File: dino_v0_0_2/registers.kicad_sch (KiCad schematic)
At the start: 5 parts, among them U31 74LS373, U32 74LS373, U33 74LS373, U34 74LS373, U35 74LS373

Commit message: Schematics WIP
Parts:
- removed U34: 74LS373, symbol 74xx:74LS373
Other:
- moved on the sheet: U35
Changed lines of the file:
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@@
-	(symbol
-		(lib_id "74xx:74LS373")
-		(at 181.61 102.87 0)
-		(mirror y)
-		(unit 1)
-		(exclude_from_sim no)
-		(in_bom yes)
-		(on_board yes)
-		(dnp no)
-		(property "Reference" "U34"
-			(at 179.4667 82.55 0)
-			(effects
-				(font
-					(size 1.27 1.27)
-				)
-				(justify left)
-			)
-		)
-		(property "Value" "74LS373"
-			(at 179.4667 85.09 0)
-			(effects
-				(font
-					(size 1.27 1.27)
-				)
-				(justify left)
-			)
-		)
-		(property "Footprint" ""
-			(at 181.61 102.87 0)
-			(effects
-				(font
-					(size 1.27 1.27)
-				)
-				(hide yes)
-			)
-		)
-		(property "Datasheet" "http://www.ti.com/lit/gpn/sn74LS373"
-			(at 181.61 102.87 0)
-			(effects
-				(font
-					(size 1.27 1.27)
-				)
-				(hide yes)
-			)
-		)
-		(property "Description" "8-bit Latch, 3-state outputs"
-			(at 181.61 102.87 0)
-			(effects
-				(font
-					(size 1.27 1.27)
-				)
-				(hide yes)
-			)
-		)
-		(pin "13"
-		)
-		(pin "14"
-		)
-		(pin "17"
-		)
-		(pin "18"
-		)
-		(pin "9"
-		)
-		(pin "12"
-		)
-		(pin "15"
-		)
-		(pin "16"
-		)
-		(pin "19"
-		)
-		(pin "11"
-		)
-		(pin "1"
-		)
-		(pin "20"
-		)
-		(pin "10"
-		)
-		(pin "2"
-		)
-		(pin "5"
-		)
-		(pin "6"
-		)
-		(pin "7"
-		)
-		(pin "8"
-		)
-		(pin "3"
-		)
-		(pin "4"
-		)
-		(instances
-			(project "dino_v0_0_2"
-				(path "/e43166a5-d972-471d-b3cf-9f4f12c7f541/de772b95-eca4-4f61-9f12-d1e28130490b"
-					(reference "U34")
-					(unit 1)
-				)
-			)
-		)
-	)
 	(symbol
 		(lib_id "74xx:74LS373")
@@
 	(symbol
 		(lib_id "74xx:74LS373")
-		(at 113.03 151.13 0)
+		(at 181.61 102.87 0)
+		(mirror y)
 		(unit 1)
 		(exclude_from_sim no)
@@
 		(on_board yes)
 		(dnp no)
-		(fields_autoplaced yes)
 		(property "Reference" "U35"
-			(at 115.1733 130.81 0)
+			(at 179.4667 82.55 0)
 			(effects
 				(font
@@
 		)
 		(property "Value" "74LS373"
-			(at 115.1733 133.35 0)
+			(at 179.4667 85.09 0)
 			(effects
 				(font
@@
 		)
 		(property "Footprint" ""
-			(at 113.03 151.13 0)
+			(at 181.61 102.87 0)
 			(effects
 				(font
@@
 		)
 		(property "Datasheet" "http://www.ti.com/lit/gpn/sn74LS373"
-			(at 113.03 151.13 0)
+			(at 181.61 102.87 0)
 			(effects
 				(font
@@
 		)
 		(property "Description" "8-bit Latch, 3-state outputs"
-			(at 113.03 151.13 0)
-			(effects
-				(font
+			(at 181.61 102.87 0)
+			(effects
+				(font

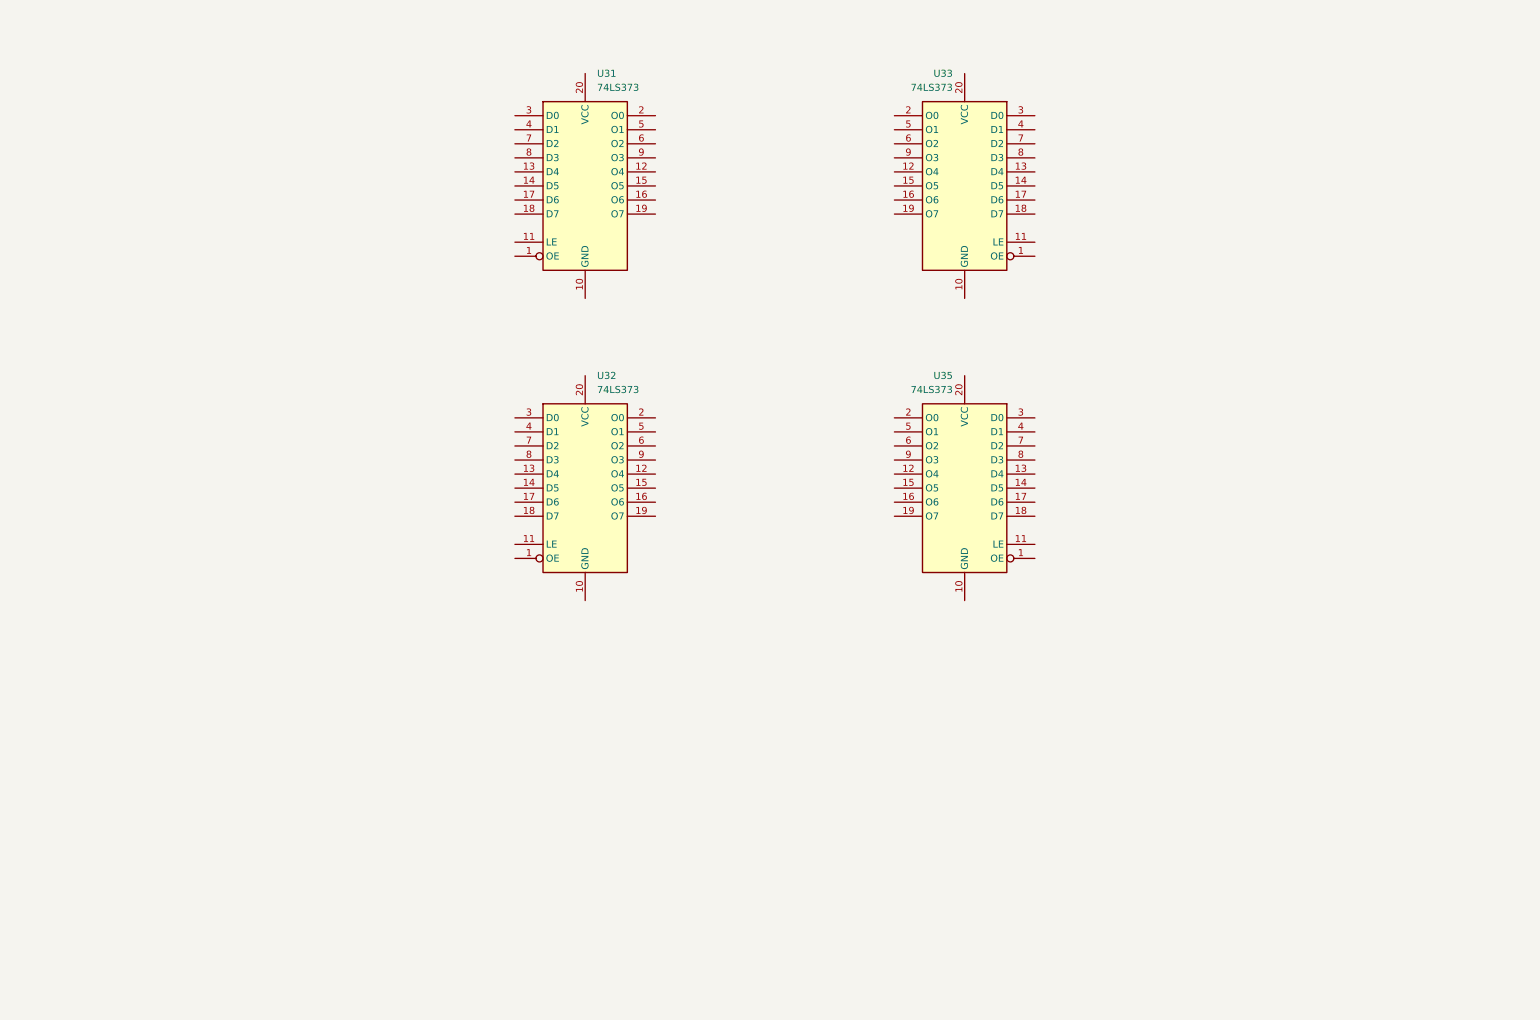
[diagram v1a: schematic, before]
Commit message: Update on Schematics
- Added the 74LS121 to the latches and RAM for intra phase pulses to allow for Latch/Write Enables
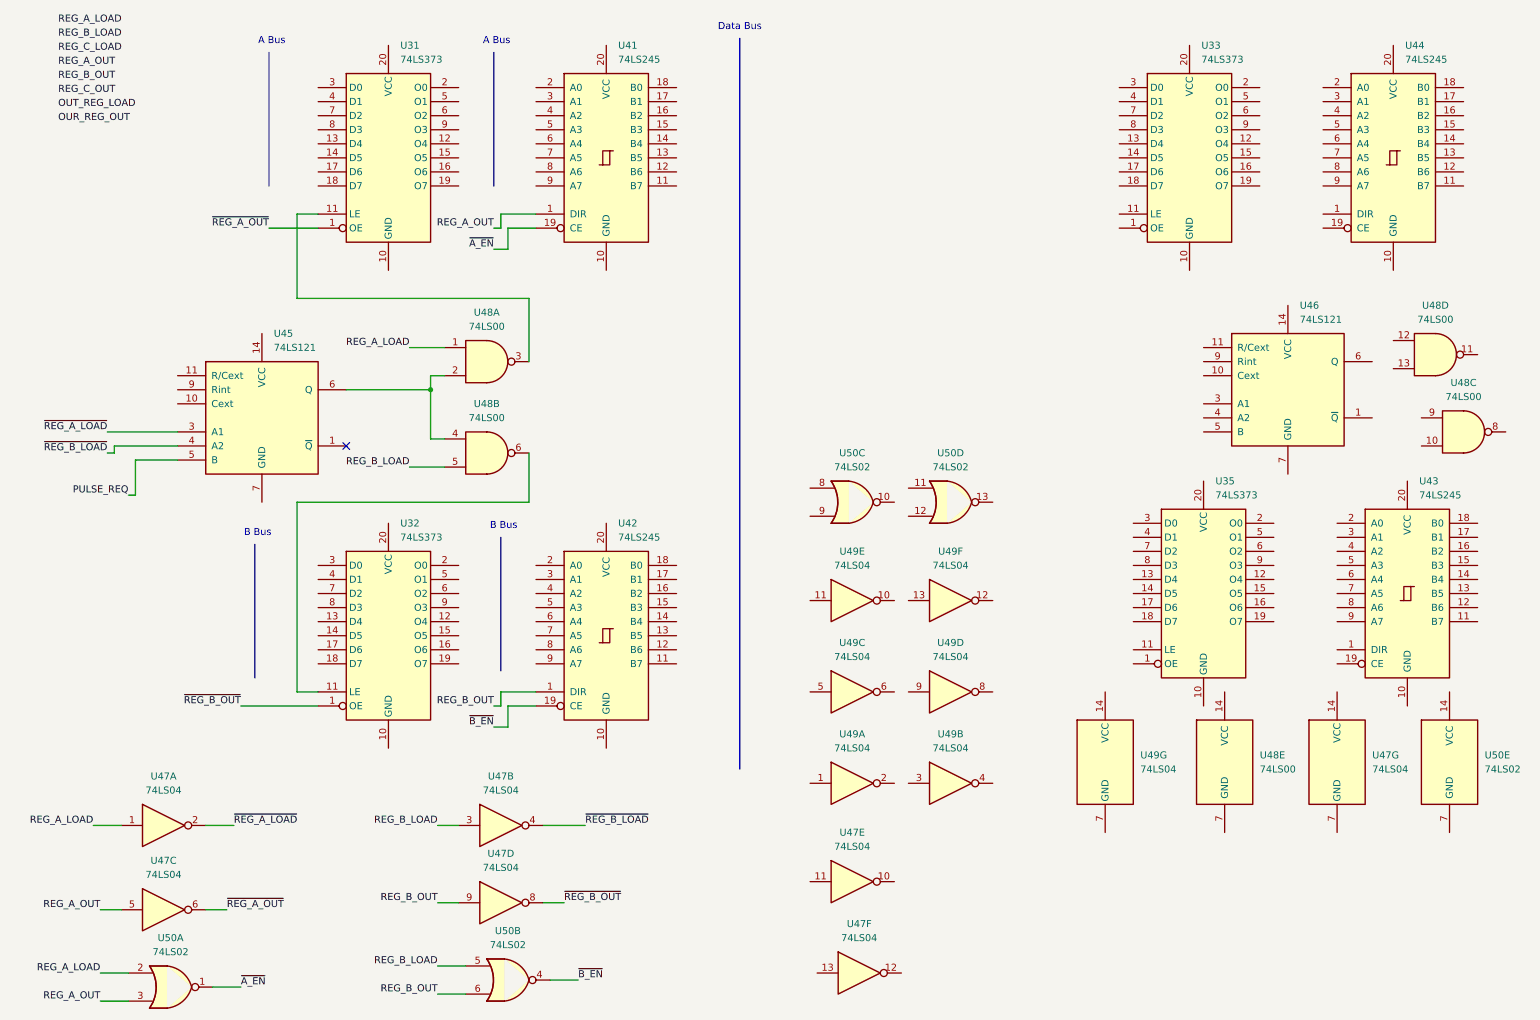
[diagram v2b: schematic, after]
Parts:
- added U41, U42, U43, U44: 74LS245, symbol 74xx:74LS245
- added U45, U46: 74LS121, symbol 74xx:74LS121
- added U47, U49: 74LS04, symbol 74xx:74LS04
- added U48: 74LS00, symbol 74xx:74LS00
- added U50: 74LS02, symbol 74xx:74LS02
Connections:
- net ~{REG_B_OUT}: now reaches U32.1 (OE)
- net ~{REG_B_OUT}: now also U47.8
- net at U32.11 (LE): now also U48.6
- net ~{REG_A_OUT}: now reaches U31.1 (OE)
- net ~{REG_A_OUT}: now also U47.6
- net at U31.11 (LE): now also U48.3
- new net: U45.6 (Q), U48.2, U48.4
- new net PULSE_REQ: U45.5 (B)
- new net REG_A_LOAD: U47.1, U48.1, U50.2
- new net REG_A_OUT: U41.1 (DIR), U47.5, U50.3
- new net REG_B_LOAD: U47.3, U48.5, U50.5
- new net REG_B_OUT: U42.1 (DIR), U47.9, U50.6
- new net ~{A_EN}: U41.19 (CE), U50.1
- new net ~{B_EN}: U42.19 (CE), U50.4
- new net ~{REG_A_LOAD}: U45.3 (A1), U47.2
- new net ~{REG_B_LOAD}: U45.4 (A2), U47.4
- no-connect marks 0 -> 1
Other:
- note added: "A Bus"
- note added: "B Bus"
- note added: "Data Bus"
- moved on the sheet: U31, U32, U33, U35
